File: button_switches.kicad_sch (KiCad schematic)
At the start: 8 parts, among them SW1 SW_Push, SW2 SW_Push, SW3 SW_Push, SW4 SW_Push

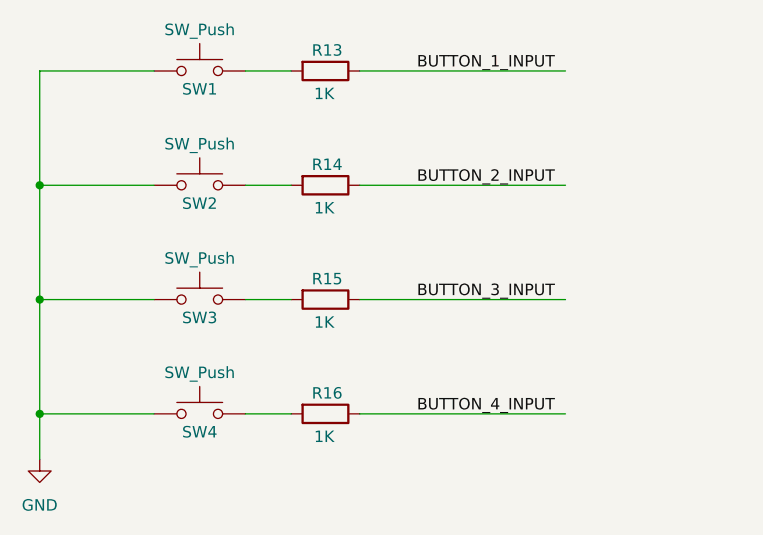
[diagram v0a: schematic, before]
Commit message: cleaned up some net labels for ERC
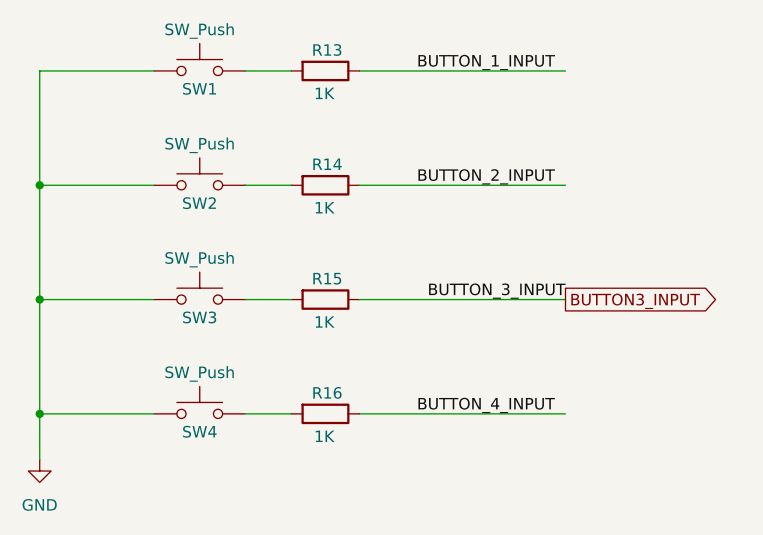
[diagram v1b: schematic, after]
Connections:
- net BUTTON_3_INPUT renamed BUTTON3_INPUT
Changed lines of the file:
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@@
 	)
 	(label "BUTTON_3_INPUT"
-		(at 148.59 88.9 0)
+		(at 165.1 88.9 180)
 		(effects
 			(font
 				(size 1.27 1.27)
 			)
-			(justify left bottom)
+			(justify right bottom)
 		)
 	)
@@
 		)
 	)
+	(global_label "BUTTON3_INPUT"
+		(shape output)
+		(at 165.1 88.9 0)
+		(fields_autoplaced yes)
+		(effects
+			(font
+				(size 1.27 1.27)
+			)
+			(justify left)
+		)
+		(property "Intersheetrefs" "${INTERSHEET_REFS}"
+			(at 182.9624 88.9 0)
+			(effects
+				(font
+					(size 1.27 1.27)
+				)
+				(justify left)
+				(hide yes)
+			)
+		)
+	)
 	(symbol
 		(lib_id "Switch:SW_Push")
@@
 		(on_board yes)
 		(dnp no)
-		(property "Reference" "#PWR039"
+		(property "Reference" "#PWR041"
 			(at 106.68 113.03 0)
 			(effects
@@
 			(project "2tonewatch"
 				(path "/29eb74dc-e91c-4cc5-ad9f-7f8caf36d690/4af52688-bac3-4b0c-b181-6834dd06dad9"
-					(reference "#PWR039")
-					(unit 1)
-				)
+					(reference "#PWR041")
+					(unit 1)
+				)

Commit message: Cleaned up local vs. global net labels
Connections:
- net BUTTON_1_INPUT renamed BUTTON1_INPUT
- net BUTTON_2_INPUT renamed BUTTON2_INPUT
- net BUTTON_4_INPUT renamed BUTTON4_INPUT
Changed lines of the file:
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@@
 	(wire
 		(pts
-			(xy 142.24 101.6) (xy 165.1 101.6)
+			(xy 142.24 101.6) (xy 149.86 101.6)
 		)
 		(stroke
@@
 	(wire
 		(pts
-			(xy 142.24 76.2) (xy 165.1 76.2)
+			(xy 142.24 76.2) (xy 149.86 76.2)
 		)
 		(stroke
@@
 	(wire
 		(pts
-			(xy 142.24 63.5) (xy 165.1 63.5)
+			(xy 142.24 63.5) (xy 149.86 63.5)
 		)
 		(stroke
@@
 	(wire
 		(pts
-			(xy 142.24 88.9) (xy 165.1 88.9)
+			(xy 142.24 88.9) (xy 149.86 88.9)
 		)
 		(stroke
@@
 		)
 	)
-	(label "BUTTON_3_INPUT"
-		(at 165.1 88.9 180)
-		(effects
-			(font
-				(size 1.27 1.27)
-			)
-			(justify right bottom)
-		)
-	)
-	(label "BUTTON_2_INPUT"
-		(at 148.59 76.2 0)
-		(effects
-			(font
-				(size 1.27 1.27)
-			)
-			(justify left bottom)
-		)
-	)
-	(label "BUTTON_1_INPUT"
-		(at 148.59 63.5 0)
-		(effects
-			(font
-				(size 1.27 1.27)
-			)
-			(justify left bottom)
-		)
-	)
-	(label "BUTTON_4_INPUT"
-		(at 148.59 101.6 0)
-		(effects
-			(font
-				(size 1.27 1.27)
-			)
-			(justify left bottom)
-		)
-	)
 	(global_label "BUTTON3_INPUT"
 		(shape output)
-		(at 165.1 88.9 0)
+		(at 149.86 88.9 0)
 		(fields_autoplaced yes)
 		(effects
@@
 		)
 		(property "Intersheetrefs" "${INTERSHEET_REFS}"
-			(at 182.9624 88.9 0)
+			(at 167.7224 88.9 0)
 			(effects
 				(font
+					(size 1.27 1.27)
+				)
+				(justify left)
+				(hide yes)
+			)
+		)
+	)
+	(global_label "BUTTON1_INPUT"
+		(shape output)
+		(at 149.86 63.5 0)
+		(fields_autoplaced yes)
+		(effects
+			(font
+				(size 1.27 1.27)
+			)
+			(justify left)
+		)
+		(property "Intersheetrefs" "${INTERSHEET_REFS}"
+			(at 167.7224 63.5 0)
+			(effects
+				(font
+					(size 1.27 1.27)
+				)
+				(justify left)
+				(hide yes)
+			)
+		)
+	)
+	(global_label "BUTTON2_INPUT"
+		(shape output)
+		(at 149.86 76.2 0)
+		(fields_autoplaced yes)
+		(effects
+			(font
+				(size 1.27 1.27)
+			)
+			(justify left)
+		)
+		(property "Intersheetrefs" "${INTERSHEET_REFS}"
+			(at 167.7224 76.2 0)
+			(effects
+				(font
+					(size 1.27 1.27)
+				)
+				(justify left)
+				(hide yes)
+			)
+		)
+	)
+	(global_label "BUTTON4_INPUT"
+		(shape output)
+		(at 149.86 101.6 0)
+		(fields_autoplaced yes)
+		(effects
+			(font
+				(size 1.27 1.27)
+			)
+			(justify left)
+		)
+		(property "Intersheetrefs" "${INTERSHEET_REFS}"
+			(at 167.7224 101.6 0)
+			(effects
+				(font

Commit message: Choose footprints for all parts
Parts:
- R11: renamed from R13; footprint (none) -> Resistor_SMD:R_0402_1005Metric
- R12: renamed from R14; footprint (none) -> Resistor_SMD:R_0402_1005Metric
- R13: renamed from R15; footprint (none) -> Resistor_SMD:R_0402_1005Metric
- R14: renamed from R16; footprint (none) -> Resistor_SMD:R_0402_1005Metric
- SW1, SW2, SW3, SW4: footprint (none) -> Button_Switch_SMD:SW_SPST_B3U-3000P; MPN (none) -> B3U-3000P
